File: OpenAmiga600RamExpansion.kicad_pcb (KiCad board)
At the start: 2 copper layers, 84.3 x 48.3 mm, 21 parts, among them J1 Conn_01x02, J99 OSHW_LOGO, U1 NEC_424260, U2 NEC_424260, U3 MSM6242B

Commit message: Reposition some RTC components
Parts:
- J1: footprint Pin_Headers:Pin_Header_Straight_1x02_Pitch2.54mm -> OpenAmiga600RamExpansion:Pin_Header_Straight_1x02-ModSilkS
- moved R4 10.00 mm to (184.3, 73.4), turned to 0 degrees
- moved R5 9.88 mm to (184.3, 75.9), turned to 0 degrees
- moved D1 3.69 mm to (188.7, 74.7), turned to 90 degrees
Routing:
- net VCC: track 171.8 -> 154.8 mm
- net Net-(BT1-Pad1): track 5.40 -> 21.4 mm
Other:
- board text added: "CLOCK ENABLE"

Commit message: Minor silkscreen fixes
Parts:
- renumbered R3 to R1, R1 to R3, R5 to R4, R4 to R5
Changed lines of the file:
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@@
   (general
     (links 120)
-    (no_connects 0)
+    (no_connects 23)
     (area 114.224999 53.264999 198.703001 101.675001)
     (thickness 1.6)
-    (drawings 15)
+    (drawings 19)
     (tracks 826)
     (zones 0)
@@
     (39 F.Mask user)
     (44 Edge.Cuts user)
-    (49 F.Fab user)
+    (49 F.Fab user hide)
   )
   (setup
@@
     (fp_arc (start 3.81 -1.39) (end 2.81 -1.39) (angle -180) (layer F.SilkS) (width 0.12))
     (pad 1 thru_hole rect (at 0 0) (size 1.6 1.6) (drill 0.8) (layers *.Cu *.Mask)
-      (net 50 "Net-(R1-Pad2)"))
+      (net 47 "Net-(R3-Pad2)"))
     (pad 10 thru_hole oval (at 7.62 20.32) (size 1.6 1.6) (drill 0.8) (layers *.Cu *.Mask)
       (net 3 /rtc_wr))
@@
       (net 6 /rtc_d3))
     (pad 3 thru_hole oval (at 0 5.08) (size 1.6 1.6) (drill 0.8) (layers *.Cu *.Mask)
-      (net 47 "Net-(R3-Pad2)"))
+      (net 50 "Net-(R1-Pad2)"))
     (pad 12 thru_hole oval (at 7.62 15.24) (size 1.6 1.6) (drill 0.8) (layers *.Cu *.Mask)
       (net 8 /rtc_d2))
@@
       (net 9 /rtc_a2))
     (pad 15 thru_hole oval (at 7.62 7.62) (size 1.6 1.6) (drill 0.8) (layers *.Cu *.Mask)
-      (net 47 "Net-(R3-Pad2)"))
+      (net 50 "Net-(R1-Pad2)"))
     (pad 7 thru_hole oval (at 0 15.24) (size 1.6 1.6) (drill 0.8) (layers *.Cu *.Mask)
       (net 4 /rtc_a3))
@@
     (tags "resistor 0805")
     (attr smd)
+    (fp_text reference R1 (at -3.302 0) (layer B.SilkS)
+      (effects (font (size 1 1) (thickness 0.15)) (justify mirror))
+    )
+    (fp_text value 10k (at 0 -1.75) (layer B.Fab)
+      (effects (font (size 1 1) (thickness 0.15)) (justify mirror))
+    )
+    (fp_text user %R (at 0 0) (layer B.Fab)
+      (effects (font (size 0.5 0.5) (thickness 0.075)) (justify mirror))
+    )
+    (fp_line (start -1 -0.62) (end -1 0.62) (layer B.Fab) (width 0.1))
+    (fp_line (start 1 -0.62) (end -1 -0.62) (layer B.Fab) (width 0.1))
+    (fp_line (start 1 0.62) (end 1 -0.62) (layer B.Fab) (width 0.1))
+    (fp_line (start -1 0.62) (end 1 0.62) (layer B.Fab) (width 0.1))
+    (fp_line (start 0.6 -0.88) (end -0.6 -0.88) (layer B.SilkS) (width 0.12))
+    (fp_line (start -0.6 0.88) (end 0.6 0.88) (layer B.SilkS) (width 0.12))
+    (fp_line (start -2.35 0.9) (end 2.35 0.9) (layer B.CrtYd) (width 0.05))
+    (fp_line (start -2.35 0.9) (end -2.35 -0.9) (layer B.CrtYd) (width 0.05))
+    (fp_line (start 2.35 -0.9) (end 2.35 0.9) (layer B.CrtYd) (width 0.05))
+    (fp_line (start 2.35 -0.9) (end -2.35 -0.9) (layer B.CrtYd) (width 0.05))
+    (pad 1 smd rect (at -1.35 0) (size 1.5 1.3) (layers B.Cu B.Mask)
+      (net 1 VCC))
+    (pad 2 smd rect (at 1.35 0) (size 1.5 1.3) (layers B.Cu B.Mask)
+      (net 50 "Net-(R1-Pad2)"))
+    (model ${KISYS3DMOD}/Resistors_SMD.3dshapes/R_0805.wrl
+      (at (xyz 0 0 0))
+      (scale (xyz 1 1 1))
+      (rotate (xyz 0 0 0))
+    )
+  )
+  (module Resistors_SMD:R_0805_HandSoldering (layer B.Cu)
+    (at 184.277 78.486)
+    (descr "Resistor SMD 0805, hand soldering")
+    (tags "resistor 0805")
+    (attr smd)
     (fp_text reference R3 (at -3.302 0) (layer B.SilkS)
       (effects (font (size 1 1) (thickness 0.15)) (justify mirror))
@@
   )
   (module Resistors_SMD:R_0805_HandSoldering (layer B.Cu)
-    (at 184.277 78.486)
-    (descr "Resistor SMD 0805, hand soldering")
-    (tags "resistor 0805")
-    (attr smd)
-    (fp_text reference R1 (at -3.302 0) (layer B.SilkS)
-      (effects (font (size 1 1) (thickness 0.15)) (justify mirror))
-    )
-    (fp_text value 10k (at 0 -1.75) (layer B.Fab)
-      (effects (font (size 1 1) (thickness 0.15)) (justify mirror))
-    )
-    (fp_text user %R (at 0 0) (layer B.Fab)
-      (effects (font (size 0.5 0.5) (thickness 0.075)) (justify mirror))
-    )
-    (fp_line (start -1 -0.62) (end -1 0.62) (layer B.Fab) (width 0.1))
-    (fp_line (start 1 -0.62) (end -1 -0.62) (layer B.Fab) (width 0.1))
-    (fp_line (start 1 0.62) (end 1 -0.62) (layer B.Fab) (width 0.1))
-    (fp_line (start -1 0.62) (end 1 0.62) (layer B.Fab) (width 0.1))
-    (fp_line (start 0.6 -0.88) (end -0.6 -0.88) (layer B.SilkS) (width 0.12))
-    (fp_line (start -0.6 0.88) (end 0.6 0.88) (layer B.SilkS) (width 0.12))
-    (fp_line (start -2.35 0.9) (end 2.35 0.9) (layer B.CrtYd) (width 0.05))
-    (fp_line (start -2.35 0.9) (end -2.35 -0.9) (layer B.CrtYd) (width 0.05))
-    (fp_line (start 2.35 -0.9) (end 2.35 0.9) (layer B.CrtYd) (width 0.05))
-    (fp_line (start 2.35 -0.9) (end -2.35 -0.9) (layer B.CrtYd) (width 0.05))
-    (pad 1 smd rect (at -1.35 0) (size 1.5 1.3) (layers B.Cu B.Mask)
-      (net 1 VCC))
-    (pad 2 smd rect (at 1.35 0) (size 1.5 1.3) (layers B.Cu B.Mask)
-      (net 50 "Net-(R1-Pad2)"))
-    (model ${KISYS3DMOD}/Resistors_SMD.3dshapes/R_0805.wrl
-      (at (xyz 0 0 0))
-      (scale (xyz 1 1 1))
-      (rotate (xyz 0 0 0))
-    )
-  )
-  (module Resistors_SMD:R_0805_HandSoldering (layer B.Cu)
     (at 184.277715 73.406)
     (descr "Resistor SMD 0805, hand soldering")
     (tags "resistor 0805")
     (attr smd)
-    (fp_text reference R4 (at -3.302 0) (layer B.SilkS)
+    (fp_text reference R5 (at -3.302 0) (layer B.SilkS)
       (effects (font (size 1 1) (thickness 0.15)) (justify mirror))
     )
@@
     (tags "resistor 0805")
     (attr smd)
-    (fp_text reference R5 (at -3.302 0) (layer B.SilkS)
+    (fp_text reference R4 (at -3.302 0) (layer B.SilkS)
       (effects (font (size 1 1) (thickness 0.15)) (justify mirror))
     )
@@
     )
   )
+  (gr_line (start 191.389 69.596) (end 197.358 69.596) (layer B.SilkS) (width 0.15))
+  (gr_line (start 191.389 75.692) (end 191.389 69.596) (layer B.SilkS) (width 0.15))
+  (gr_line (start 197.358 75.692) (end 191.389 75.692) (layer B.SilkS) (width 0.15))
+  (gr_line (start 197.358 69.596) (end 197.358 75.692) (layer B.SilkS) (width 0.15))
   (gr_text "CLOCK\nENABLE" (at 193.294 72.644 90) (layer B.SilkS)
     (effects (font (size 1 1) (thickness 0.15)) (justify mirror))
@@
   (segment (start 188.468 81.026) (end 187.33663 81.026) (width 0.25) (layer B.Cu) (net 46))
   (segment (start 187.33663 81.026) (end 185.627 81.026) (width 0.25) (layer B.Cu) (net 46))
-  (segment (start 196.088 86.106) (end 191.008 86.106) (width 0.254) (layer B.Cu) (net 47))
-  (segment (start 191.008 86.106) (end 188.468 83.566) (width 0.254) (layer B.Cu) (net 47))
-  (segment (start 188.468 83.566) (end 185.627 83.566) (width 0.25) (layer B.Cu) (net 47))
+  (segment (start 188.468 78.486) (end 185.627 78.486) (width 0.25) (layer B.Cu) (net 47))
   (segment (start 190.627 74.676) (end 189.77864 74.676) (width 0.4) (layer B.Cu) (net 48))
   (segment (start 191.135 77.268) (end 191.135 78.518) (width 0.4) (layer B.Cu) (net 48))
@@
   (segment (start 196.403 65.151) (end 183.515 65.151) (width 0.4) (layer B.Cu) (net 49))
   (segment (start 182.927715 65.738285) (end 182.927715 73.406) (width 0.4) (layer B.Cu) (net 49))
-  (segment (start 188.468 78.486) (end 185.627 78.486) (width 0.25) (layer B.Cu) (net 50))
+  (segment (start 196.088 86.106) (end 191.008 86.106) (width 0.254) (layer B.Cu) (net 50))
+  (segment (start 191.008 86.106) (end 188.468 83.566) (width 0.254) (layer B.Cu) (net 50))
+  (segment (start 188.468 83.566) (end 185.627 83.566) (width 0.25) (layer B.Cu) (net 50))
   (zone (net 2) (net_name GND) (layer F.Cu) (hatch edge 0.508)
     (connect_pads (clearance 0.1))

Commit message: The sweetest perfection ;)
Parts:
- added D2: LED, LED_0805_HandSoldering_ModSilkS, B.Cu at (172.8, 94.6)
- added R6: 1K, Resistors_SMD:R_0805_HandSoldering, B.Cu at (172.8, 97.2)
- moved J99 0.28 mm to (120.7, 58.5)
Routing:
- net VCC: track 154.8 -> 161.0 mm, vias 1 -> 2
- net Net-(D2-Pad2): track 0.00 -> 2.54 mm
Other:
- board text added: "POWER LED"

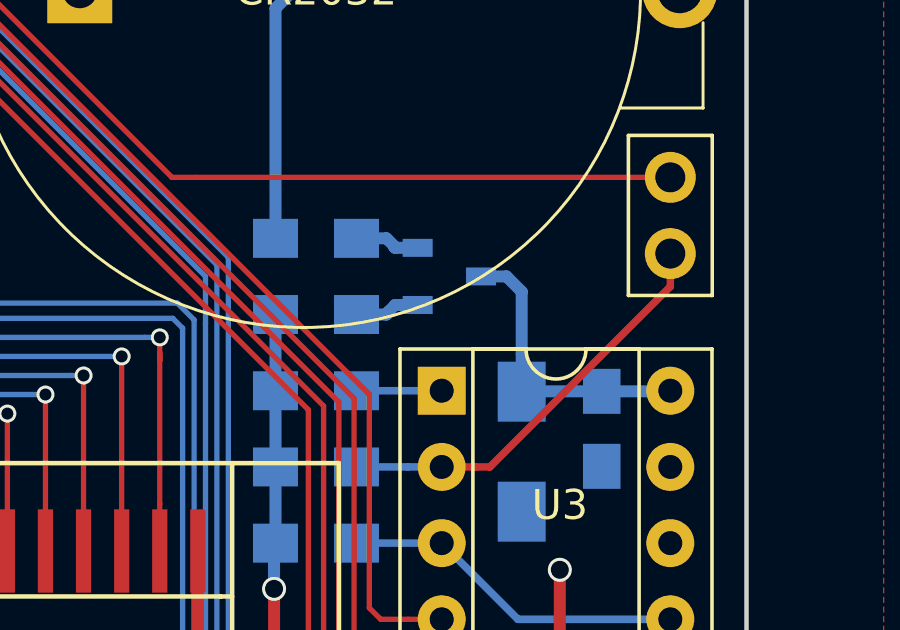
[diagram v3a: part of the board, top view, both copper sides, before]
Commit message: Use HandSoldering version of SOT-23 footprint
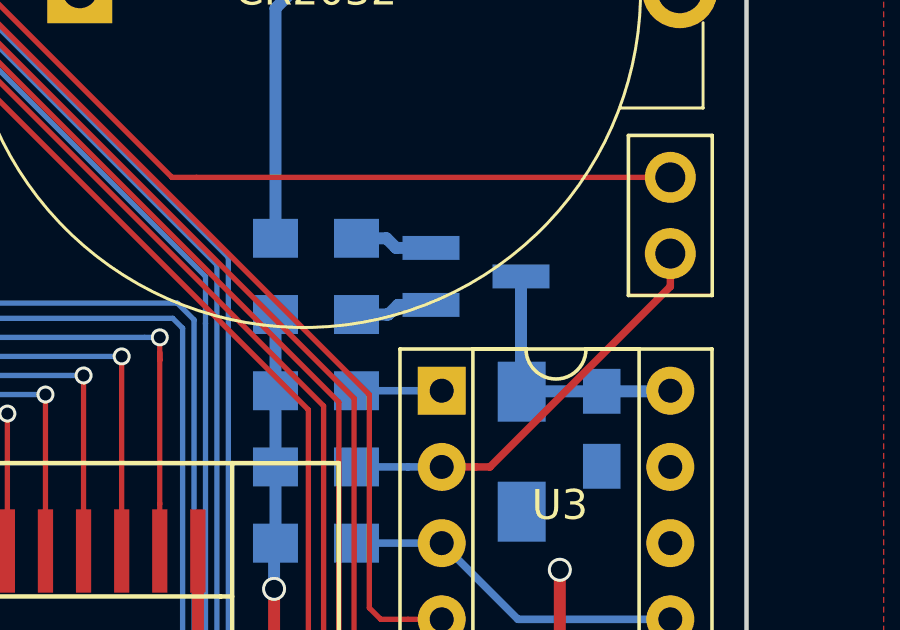
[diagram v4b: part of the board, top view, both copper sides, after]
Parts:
- D1: footprint smd_trans:sot23 -> TO_SOT_Packages_SMD:SOT-23_Handsoldering
- D2: footprint LED_0805_HandSoldering_ModSilkS -> OpenAmiga600RamExpansion:LED_0805_HandSoldering_ModSilkS
- moved D1 0.89 mm to (189.6, 74.7), turned to 0 degrees
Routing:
- net VDD: track 9.87 -> 8.82 mm

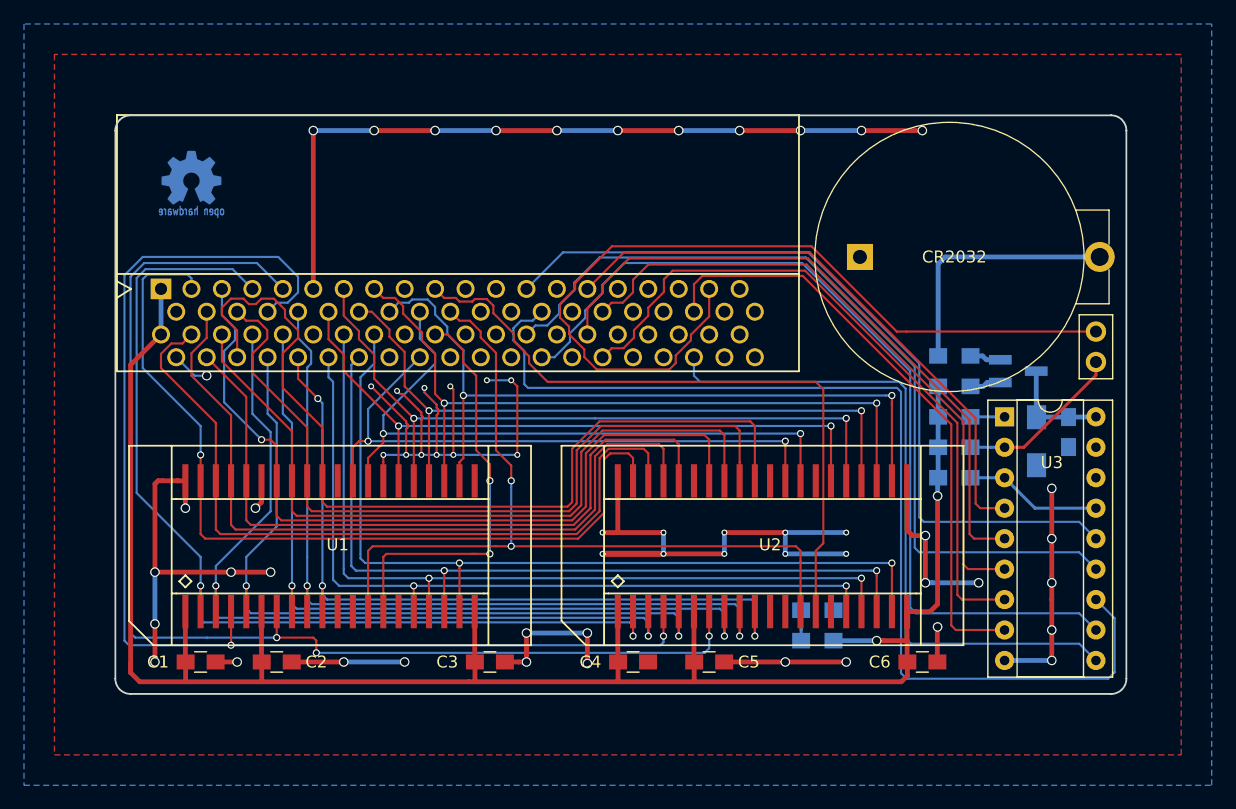
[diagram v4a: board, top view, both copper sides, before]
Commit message: Switch to KiCad 5
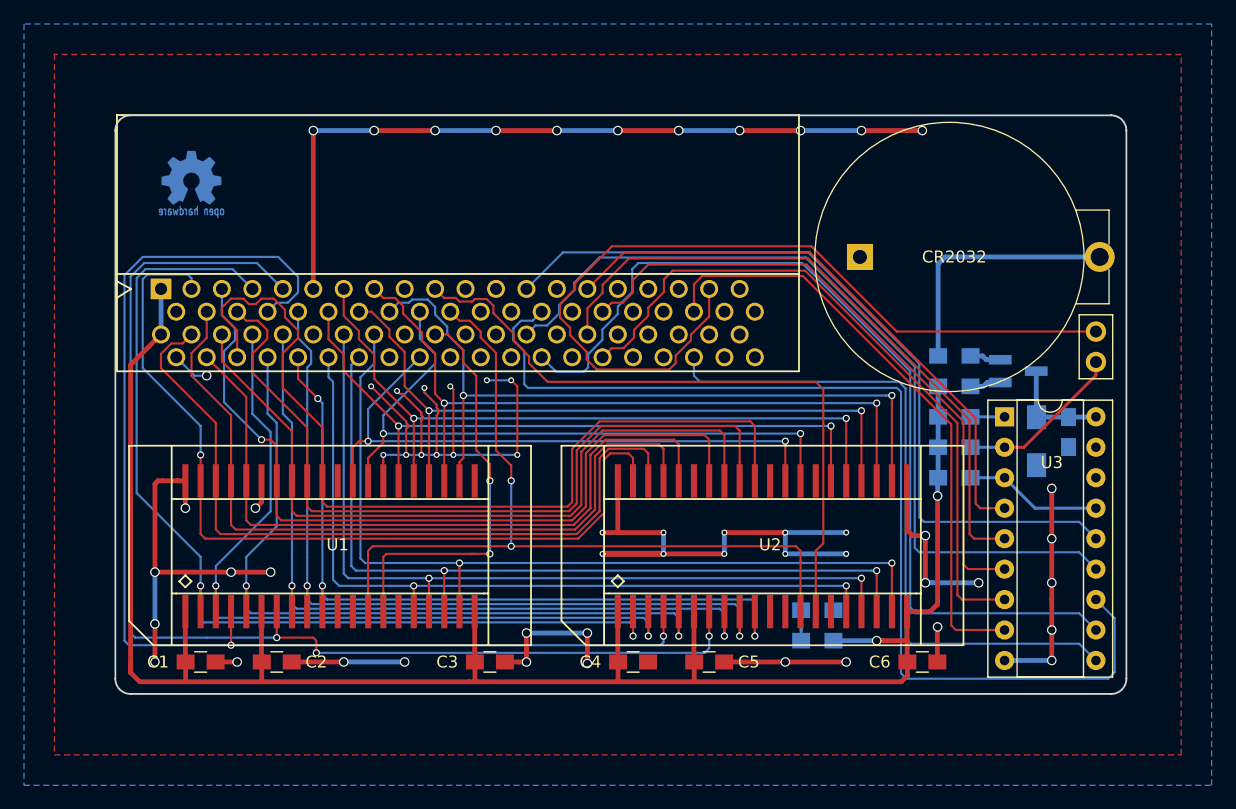
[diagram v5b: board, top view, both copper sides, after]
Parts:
- renumbered D2 to L1
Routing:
- net /rtc_d3: track 74.9 -> 77.4 mm
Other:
- net class Default: clearance 0.178 -> 0.15
- net class Power: clearance 0.25 -> 0.15
- net class Thin: clearance 0.2 -> 0.15
- rule trace_clearance: 0.178 -> 0.15

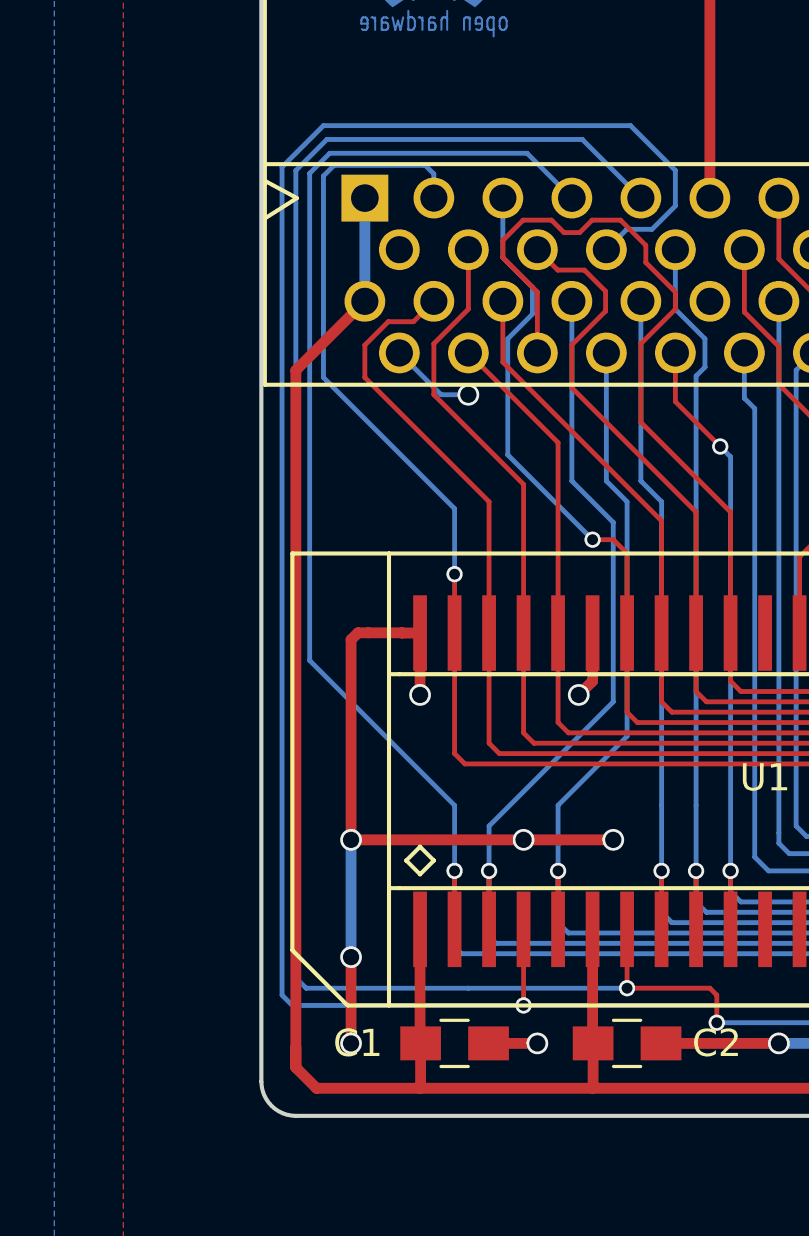
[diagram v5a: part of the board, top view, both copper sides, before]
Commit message: Add (optional) decoupling electrolytic cap, just in case
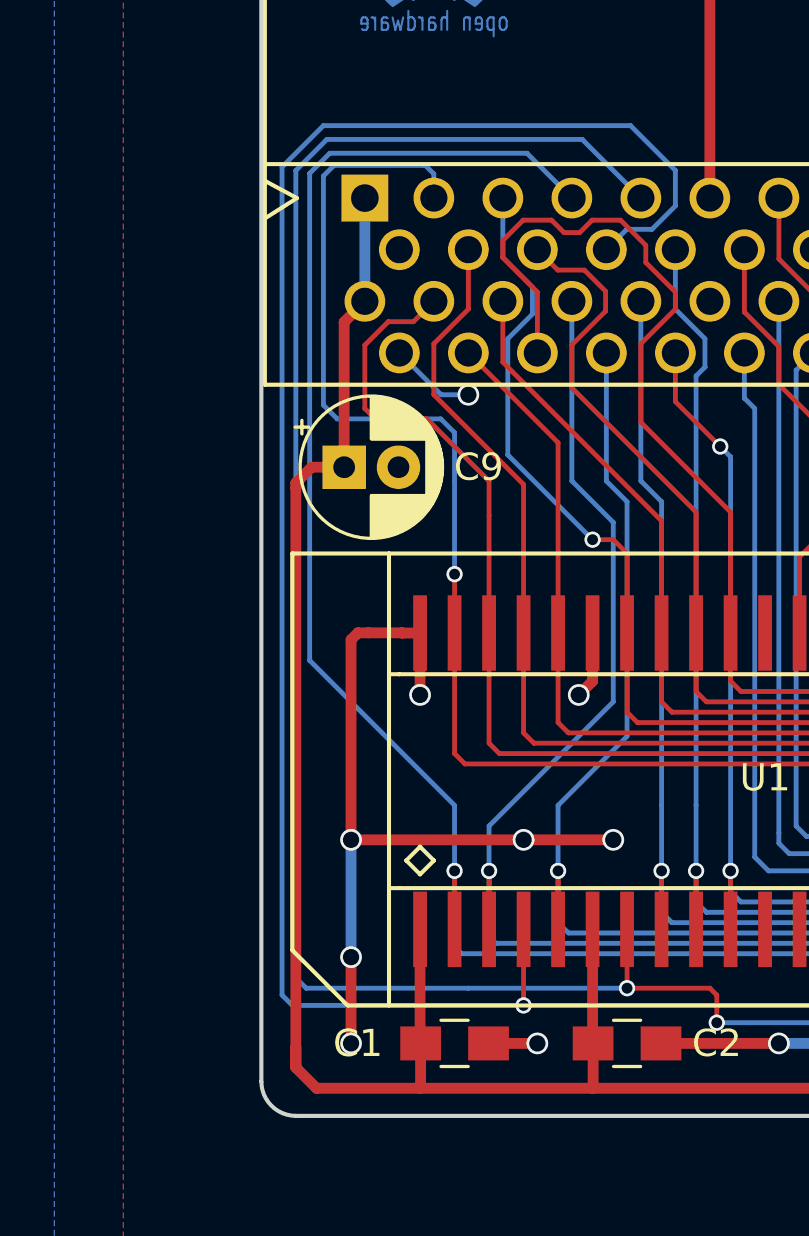
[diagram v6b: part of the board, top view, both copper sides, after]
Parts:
- added C9: 10uF, Capacitor_THT:CP_Radial_D5.0mm_P2.00mm, F.Cu at (117.3, 77.7)
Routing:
- net /d15: track 72.3 -> 74.6 mm
- net /d14: track 64.0 -> 65.1 mm
- net VCC: track 161.0 -> 161.7 mm

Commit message: Add license
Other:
- board text added: "github.com/SukkoPera/OpenAmiga600RamExpansion Licensed under CERN OHL v.1.2"
- board text removed: "github.com/SukkoPera/OpenAmiga600RamExpansion"
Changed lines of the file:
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@@
-(kicad_pcb (version 20171130) (host pcbnew 5.0.0)
+(kicad_pcb (version 20171130) (host pcbnew 5.1.2)
   (general
     (thickness 1.6)
@@
     (rev 1)
     (company SukkoPera)
+    (comment 1 "Licensed under CERN OHL v.1.2")
   )
   (layers
@@
     (zone_45_only no)
     (trace_min 0.1524)
-    (segment_width 0.15)
-    (edge_width 0.15)
     (via_size 0.6)
     (via_drill 0.4)
@@
     (uvia_min_size 0.2)
     (uvia_min_drill 0.1)
+    (edge_width 0.15)
+    (segment_width 0.15)
     (pcb_text_width 0.3)
     (pcb_text_size 1.5 1.5)
@@
     (visible_elements FFFFFF7F)
     (pcbplotparams
-      (layerselection 0x010f0_80000001)
+      (layerselection 0x010f0_ffffffff)
       (usegerberextensions false)
       (usegerberattributes false)
@@
     (effects (font (size 1 1) (thickness 0.15)) (justify mirror))
   )
-  (gr_text github.com/SukkoPera/OpenAmiga600RamExpansion (at 156.46 58.928) (layer B.SilkS)
+  (gr_text "github.com/SukkoPera/OpenAmiga600RamExpansion\nLicensed under CERN OHL v.1.2" (at 156.464 59.436) (layer B.SilkS)
     (effects (font (size 1 1) (thickness 0.15)) (justify mirror))
   )
